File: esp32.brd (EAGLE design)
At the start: 123.5 x 80.4 mm, 12 parts, among them IC1 LM1117IMPX-3.3, U1 ESP32MOD

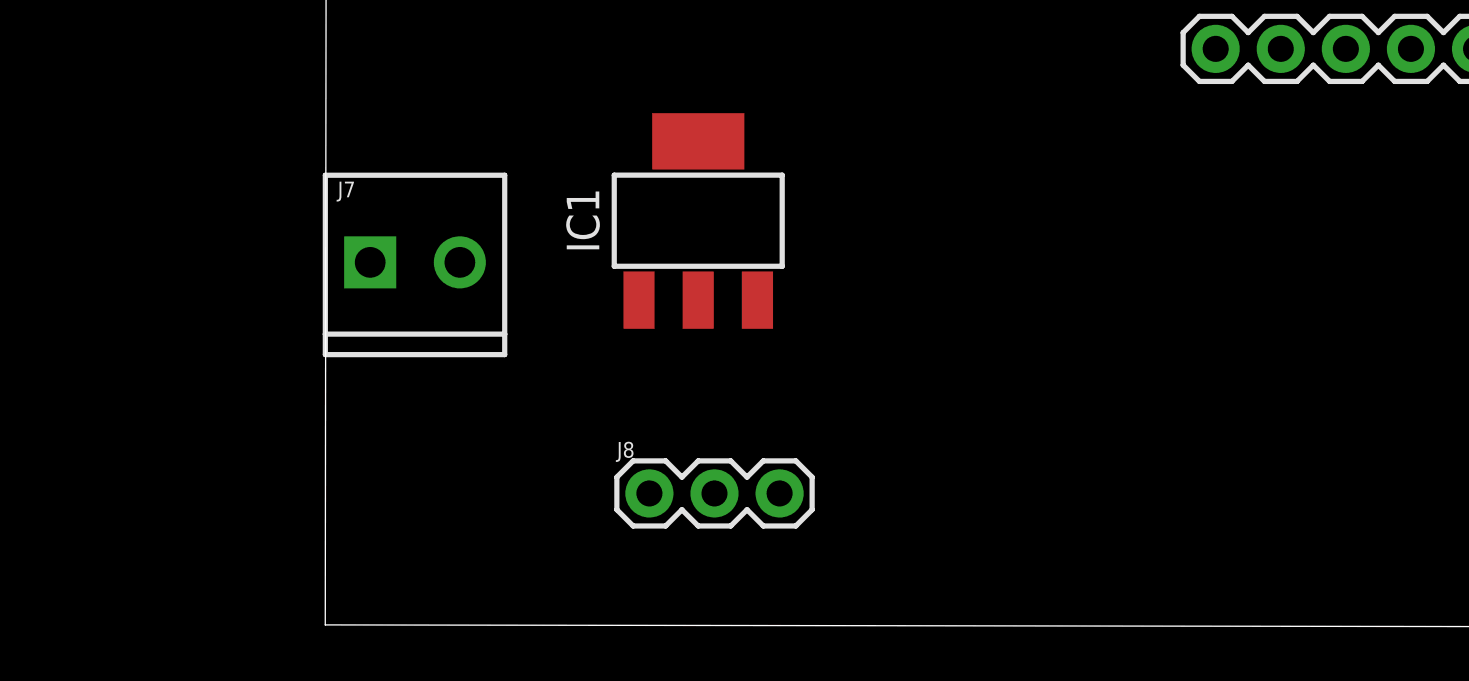
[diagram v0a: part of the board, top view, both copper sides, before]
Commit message: Added the reset circuitry
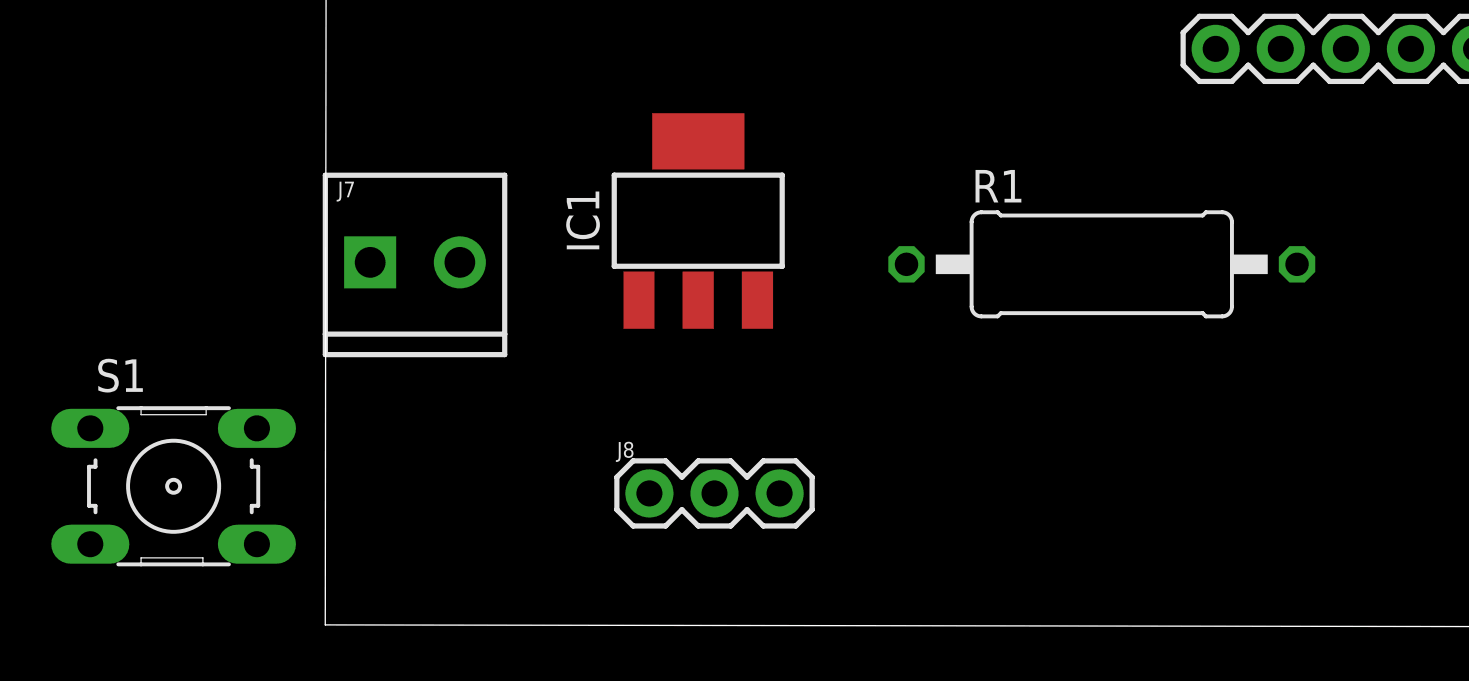
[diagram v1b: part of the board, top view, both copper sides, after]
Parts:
- added R1: (no value), rcl:0411/15
- added S1: (no value), switch-omron:B3F-10XX
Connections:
- removed net N$4: J1.13, J4.13, U1.2
- removed net N$5: J1.12, J4.12, U1.3
- new net RST: J1.12, J4.12, R1.2, S1.1, S1.2, U1.3
- net 3.3V: now also J1.13, J4.13, R1.1, U1.2
- net GND: now also S1.3, S1.4
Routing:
- net N$4: track 9.35 -> 0.00 mm
- net 3.3V: track 0.00 -> 9.35 mm
- net RST: track 0.00 -> 8.82 mm
- net N$5: track 8.82 -> 0.00 mm
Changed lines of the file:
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@@
 </element>
 <element name="J8" library="SparkFun-Connectors" package="1X03" value="" x="11.1252" y="16.891"/>
+<element name="R1" library="rcl" package="0411/15" value="" x="28.7782" y="25.8318"/>
+<element name="S1" library="switch-omron" package="B3F-10XX" value="" x="-7.4422" y="17.1704">
+<attribute name="OC_FARNELL" value="176432" x="-7.4422" y="17.1704" size="1.778" layer="27" display="off"/>
+<attribute name="MPN" value="B3F-1000" x="-7.4422" y="17.1704" size="1.778" layer="27" display="off"/>
+<attribute name="OC_NEWARK" value="36M3542" x="-7.4422" y="17.1704" size="1.778" layer="27" display="off"/>
+<attribute name="MF" value="" x="-7.4422" y="17.1704" size="1.778" layer="27" display="off"/>
+</element>
 </elements>
 <signals>
@@
 <contactref element="C1" pad="1"/>
 <contactref element="J8" pad="1"/>
+<contactref element="S1" pad="3"/>
+<contactref element="S1" pad="4"/>
 <wire x1="60.96" y1="77.216" x2="72.898" y2="77.2922" width="0" layer="19" extent="1-1"/>
 <wire x1="44.444" y1="64.116" x2="53.924" y2="71.806" width="0" layer="19" extent="1-1"/>
@@
 <wire x1="14.097" y1="77.4954" x2="27.686" y2="77.47" width="0" layer="19" extent="1-1"/>
 <wire x1="10.7192" y1="24.4346" x2="33.2232" y2="34.2392" width="0" layer="19" extent="1-1"/>
+<wire x1="11.1252" y1="16.891" x2="10.7192" y2="24.4346" width="0" layer="19" extent="1-1"/>
 <wire x1="0.2286" y1="25.908" x2="10.7192" y2="24.4346" width="0" layer="19" extent="1-1"/>
+<wire x1="-4.191" y1="14.9098" x2="0.2286" y2="25.908" width="0" layer="19" extent="1-1"/>
+<wire x1="-10.6934" y1="14.9098" x2="-4.191" y2="14.9098" width="0" layer="19" extent="1-1"/>
 <wire x1="6.9342" y1="39.6494" x2="0.2286" y2="25.908" width="0" layer="19" extent="1-1"/>
 <wire x1="7.7724" y1="47.9806" x2="6.9342" y2="39.6494" width="0" layer="19" extent="1-1"/>
-<wire x1="11.1252" y1="16.891" x2="0.2286" y2="25.908" width="0" layer="19" extent="1-1"/>
-</signal>
-<signal name="N$4">
-<contactref element="J1" pad="13"/>
-<contactref element="U1" pad="2"/>
-<wire x1="32.22625" y1="70.64375" x2="35.08375" y2="70.64375" width="0.5842" layer="1"/>
-<wire x1="27.94" y1="74.93" x2="32.22625" y2="70.64375" width="0.5842" layer="1"/>
-<wire x1="27.686" y1="74.93" x2="27.94" y2="74.93" width="0.5842" layer="1"/>
-<wire x1="35.08375" y1="70.64375" x2="35.224" y2="70.536" width="0.5842" layer="1"/>
-<contactref element="J4" pad="13"/>
-<wire x1="14.097" y1="74.9554" x2="27.686" y2="74.93" width="0" layer="19" extent="1-1"/>
-</signal>
-<signal name="N$5">
+</signal>
+<signal name="RST">
 <contactref element="J1" pad="12"/>
 <contactref element="U1" pad="3"/>
@@
 <wire x1="35.08375" y1="69.37375" x2="35.224" y2="69.266" width="0.5842" layer="1"/>
 <contactref element="J4" pad="12"/>
+<contactref element="R1" pad="2"/>
+<contactref element="S1" pad="1"/>
+<contactref element="S1" pad="2"/>
 <wire x1="14.097" y1="72.4154" x2="27.686" y2="72.39" width="0" layer="19" extent="1-1"/>
+<wire x1="36.3982" y1="25.8318" x2="35.224" y2="69.266" width="0" layer="19" extent="1-1"/>
+<wire x1="-4.191" y1="19.431" x2="36.3982" y2="25.8318" width="0" layer="19" extent="1-1"/>
+<wire x1="-10.6934" y1="19.431" x2="-4.191" y2="19.431" width="0" layer="19" extent="1-1"/>
 </signal>
 <signal name="N$2">
@@
 <contactref element="C2" pad="2"/>
 <contactref element="J8" pad="2"/>
+<contactref element="R1" pad="1"/>
+<contactref element="J1" pad="13"/>
+<contactref element="U1" pad="2"/>
+<wire x1="32.22625" y1="70.64375" x2="35.08375" y2="70.64375" width="0.5842" layer="1"/>
+<wire x1="27.94" y1="74.93" x2="32.22625" y2="70.64375" width="0.5842" layer="1"/>
+<wire x1="27.686" y1="74.93" x2="27.94" y2="74.93" width="0.5842" layer="1"/>
+<wire x1="35.08375" y1="70.64375" x2="35.224" y2="70.536" width="0.5842" layer="1"/>
+<contactref element="J4" pad="13"/>
+<wire x1="14.097" y1="74.9554" x2="27.686" y2="74.93" width="0" layer="19" extent="1-1"/>
+<wire x1="9.7282" y1="39.6494" x2="14.097" y2="74.9554" width="0" layer="19" extent="1-1"/>
 <wire x1="13.0302" y1="30.6326" x2="9.7282" y2="39.6494" width="0" layer="19" extent="1-1"/>
 <wire x1="13.0302" y1="24.4346" x2="13.0302" y2="30.6326" width="0" layer="19" extent="1-1"/>
 <wire x1="13.6652" y1="16.891" x2="13.0302" y2="24.4346" width="0" layer="19" extent="1-1"/>
+<wire x1="21.1582" y1="25.8318" x2="13.0302" y2="24.4346" width="0" layer="19" extent="1-1"/>
 </signal>
 </signals>

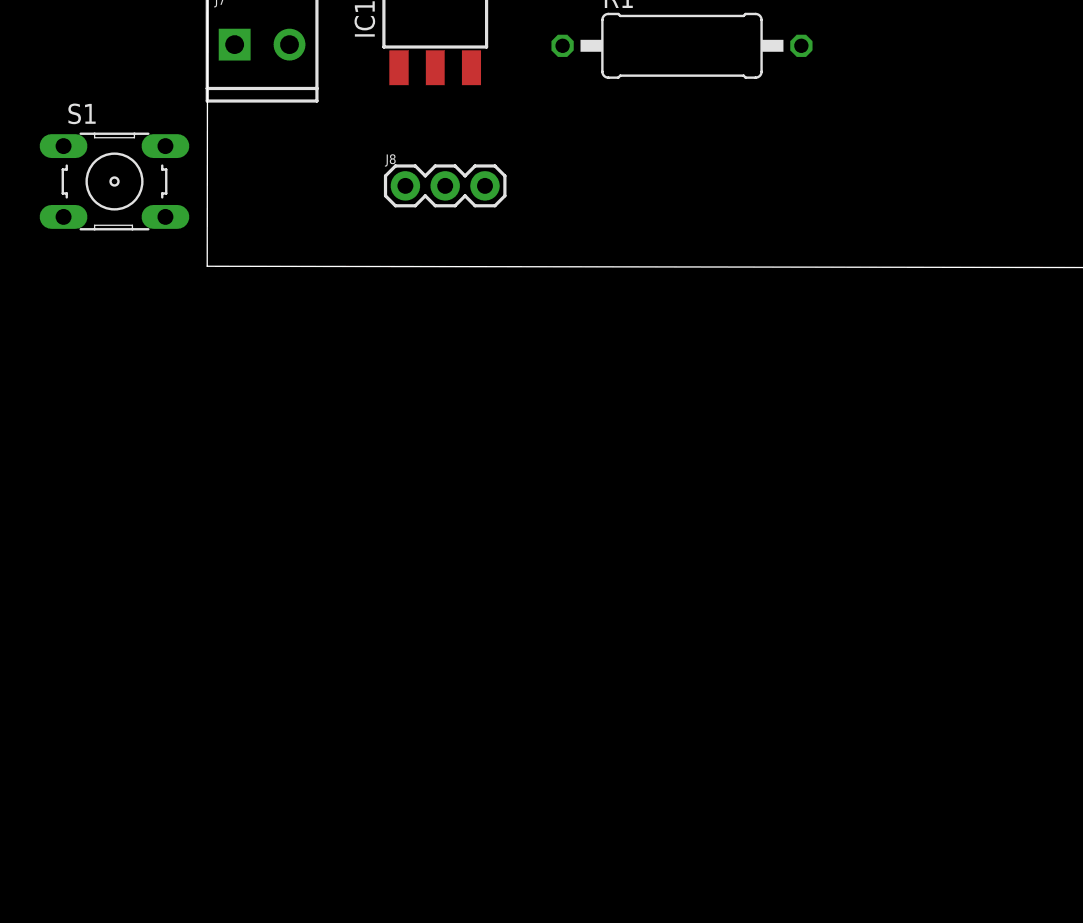
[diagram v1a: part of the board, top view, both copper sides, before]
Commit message: Added all the GPIO strapping bias resistors
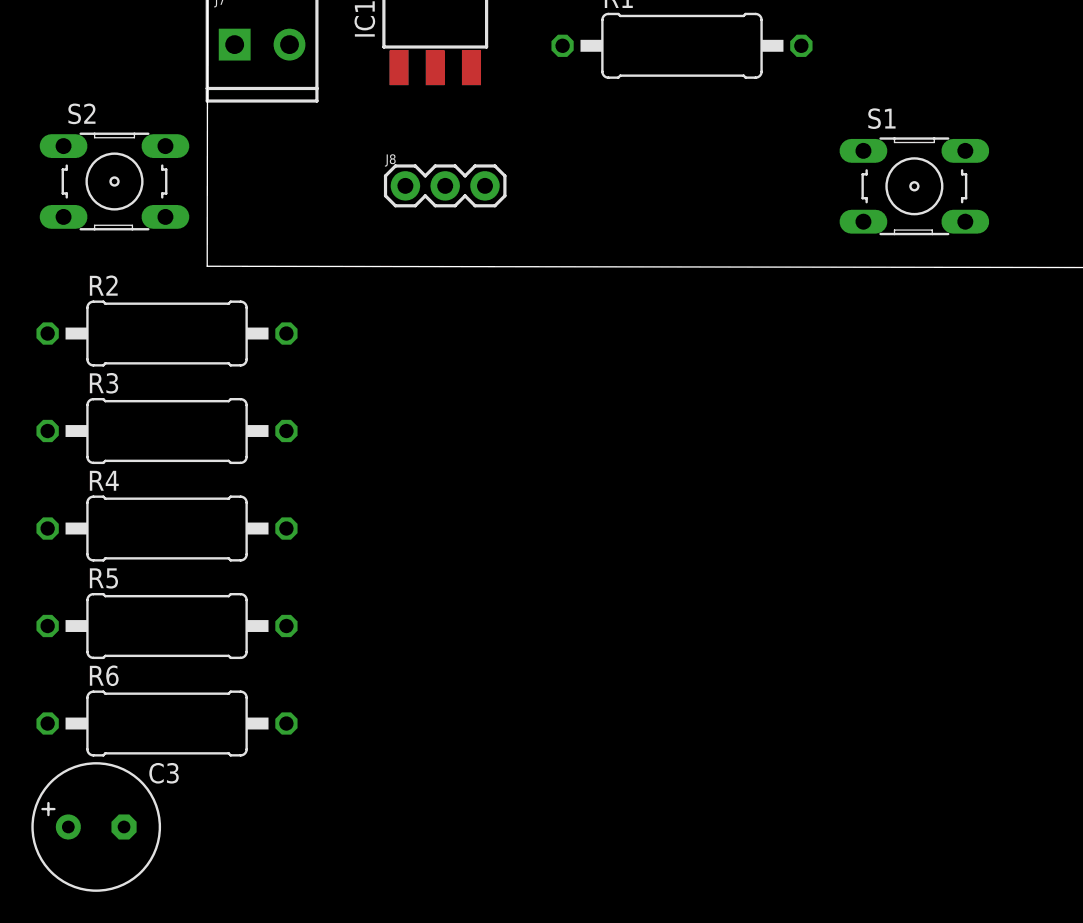
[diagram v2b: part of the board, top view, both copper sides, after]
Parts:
- added C3: (no value), rcl:E3,5-8
- added R2, R3, R4, R5, R6: 4.7k, rcl:0411/15
- added S2: (no value), switch-omron:B3F-10XX
- R1: value (none) -> 4.7k
- moved S1 51.1 mm to (43.6, 16.9)
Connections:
- net 3.3V: now also C3.+, R2.2, R5.1, R6.2
- net GND: now also C3.-, R3.2, R4.1, S2.3, S2.4
- net N$14: now also R4.2
- net N$19: now also R6.1
- net N$28: now also R2.1, S2.1, S2.2
- net N$37: now also R5.2
- net N$38: now also R3.1
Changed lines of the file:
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@@
 </element>
 <element name="J8" library="SparkFun-Connectors" package="1X03" value="" x="11.1252" y="16.891"/>
-<element name="R1" library="rcl" package="0411/15" value="" x="28.7782" y="25.8318"/>
-<element name="S1" library="switch-omron" package="B3F-10XX" value="" x="-7.4422" y="17.1704">
+<element name="R1" library="rcl" package="0411/15" value="4.7k" x="28.7782" y="25.8318"/>
+<element name="S1" library="switch-omron" package="B3F-10XX" value="" x="43.6118" y="16.8656">
+<attribute name="OC_FARNELL" value="176432" x="43.6118" y="16.8656" size="1.778" layer="27" display="off"/>
+<attribute name="MPN" value="B3F-1000" x="43.6118" y="16.8656" size="1.778" layer="27" display="off"/>
+<attribute name="OC_NEWARK" value="36M3542" x="43.6118" y="16.8656" size="1.778" layer="27" display="off"/>
+<attribute name="MF" value="" x="43.6118" y="16.8656" size="1.778" layer="27" display="off"/>
+</element>
+<element name="S2" library="switch-omron" package="B3F-10XX" value="" x="-7.4422" y="17.1704">
 <attribute name="OC_FARNELL" value="176432" x="-7.4422" y="17.1704" size="1.778" layer="27" display="off"/>
 <attribute name="MPN" value="B3F-1000" x="-7.4422" y="17.1704" size="1.778" layer="27" display="off"/>
@@
 <attribute name="MF" value="" x="-7.4422" y="17.1704" size="1.778" layer="27" display="off"/>
 </element>
+<element name="R2" library="rcl" package="0411/15" value="4.7k" x="-4.0894" y="7.4676"/>
+<element name="R3" library="rcl" package="0411/15" value="4.7k" x="-4.0894" y="1.2446"/>
+<element name="R4" library="rcl" package="0411/15" value="4.7k" x="-4.0894" y="-4.9784"/>
+<element name="R5" library="rcl" package="0411/15" value="4.7k" x="-4.0894" y="-11.2014"/>
+<element name="R6" library="rcl" package="0411/15" value="4.7k" x="-4.0894" y="-17.4244"/>
+<element name="C3" library="rcl" package="E3,5-8" value="" x="-8.6106" y="-24.0284"/>
 </elements>
 <signals>
@@
 <contactref element="S1" pad="3"/>
 <contactref element="S1" pad="4"/>
+<contactref element="S2" pad="4"/>
+<contactref element="S2" pad="3"/>
+<contactref element="R3" pad="2"/>
+<contactref element="R4" pad="1"/>
+<contactref element="C3" pad="-"/>
 <wire x1="60.96" y1="77.216" x2="72.898" y2="77.2922" width="0" layer="19" extent="1-1"/>
 <wire x1="44.444" y1="64.116" x2="53.924" y2="71.806" width="0" layer="19" extent="1-1"/>
@@
 <wire x1="33.2232" y1="34.2392" x2="33.274" y2="43.434" width="0" layer="19" extent="1-1"/>
 <wire x1="14.097" y1="77.4954" x2="27.686" y2="77.47" width="0" layer="19" extent="1-1"/>
+<wire x1="40.3606" y1="14.605" x2="33.2232" y2="34.2392" width="0" layer="19" extent="1-1"/>
+<wire x1="46.863" y1="14.605" x2="40.3606" y2="14.605" width="0" layer="19" extent="1-1"/>
 <wire x1="10.7192" y1="24.4346" x2="33.2232" y2="34.2392" width="0" layer="19" extent="1-1"/>
 <wire x1="11.1252" y1="16.891" x2="10.7192" y2="24.4346" width="0" layer="19" extent="1-1"/>
@@
 <wire x1="6.9342" y1="39.6494" x2="0.2286" y2="25.908" width="0" layer="19" extent="1-1"/>
 <wire x1="7.7724" y1="47.9806" x2="6.9342" y2="39.6494" width="0" layer="19" extent="1-1"/>
+<wire x1="3.5306" y1="1.2446" x2="-4.191" y2="14.9098" width="0" layer="19" extent="1-1"/>
+<wire x1="-11.7094" y1="-4.9784" x2="3.5306" y2="1.2446" width="0" layer="19" extent="1-1"/>
+<wire x1="-6.8326" y1="-24.0284" x2="-11.7094" y2="-4.9784" width="0" layer="19" extent="1-1"/>
 </signal>
 <signal name="RST">
@@
 <wire x1="14.097" y1="72.4154" x2="27.686" y2="72.39" width="0" layer="19" extent="1-1"/>
 <wire x1="36.3982" y1="25.8318" x2="35.224" y2="69.266" width="0" layer="19" extent="1-1"/>
-<wire x1="-4.191" y1="19.431" x2="36.3982" y2="25.8318" width="0" layer="19" extent="1-1"/>
-<wire x1="-10.6934" y1="19.431" x2="-4.191" y2="19.431" width="0" layer="19" extent="1-1"/>
+<wire x1="46.863" y1="19.1262" x2="36.3982" y2="25.8318" width="0" layer="19" extent="1-1"/>
+<wire x1="40.3606" y1="19.1262" x2="46.863" y2="19.1262" width="0" layer="19" extent="1-1"/>
 </signal>
 <signal name="N$2">
@@
 <wire x1="35.08375" y1="55.245" x2="35.224" y2="55.296" width="0.5842" layer="1"/>
 <contactref element="J4" pad="1"/>
+<contactref element="R4" pad="2"/>
 <wire x1="14.097" y1="44.4754" x2="27.686" y2="44.45" width="0" layer="19" extent="1-1"/>
+<wire x1="3.5306" y1="-4.9784" x2="14.097" y2="44.4754" width="0" layer="19" extent="1-1"/>
 </signal>
 <signal name="N$22">
@@
 <wire x1="60.96" y1="54.45125" x2="60.96" y2="54.356" width="0.5842" layer="1"/>
 <contactref element="J5" pad="10"/>
+<contactref element="R6" pad="1"/>
 <wire x1="60.96" y1="54.356" x2="72.898" y2="54.4322" width="0" layer="19" extent="1-1"/>
+<wire x1="-11.7094" y1="-17.4244" x2="53.975" y2="60.325" width="0" layer="19" extent="1-1"/>
 </signal>
 <signal name="N$15">
@@
 <wire x1="60.96" y1="44.29125" x2="60.96" y2="44.196" width="0.5842" layer="1"/>
 <contactref element="J5" pad="14"/>
+<contactref element="R2" pad="1"/>
+<contactref element="S2" pad="1"/>
+<contactref element="S2" pad="2"/>
 <wire x1="60.96" y1="44.196" x2="72.898" y2="44.2722" width="0" layer="19" extent="1-1"/>
+<wire x1="-4.191" y1="19.431" x2="53.975" y2="50.95875" width="0" layer="19" extent="1-1"/>
+<wire x1="-10.6934" y1="19.431" x2="-4.191" y2="19.431" width="0" layer="19" extent="1-1"/>
+<wire x1="-11.7094" y1="7.4676" x2="-10.6934" y2="19.431" width="0" layer="19" extent="1-1"/>
 </signal>
 <signal name="N$30">
@@
 <wire x1="53.49875" y1="43.4975" x2="53.594" y2="43.434" width="0.5842" layer="1"/>
 <contactref element="J6" pad="2"/>
+<contactref element="R5" pad="2"/>
 <wire x1="53.5432" y1="34.2392" x2="53.594" y2="43.434" width="0" layer="19" extent="1-1"/>
+<wire x1="3.5306" y1="-11.2014" x2="53.5432" y2="34.2392" width="0" layer="19" extent="1-1"/>
 </signal>
 <signal name="N$38">
@@
 <wire x1="56.03875" y1="43.4975" x2="56.134" y2="43.434" width="0.5842" layer="1"/>
 <contactref element="J6" pad="1"/>
+<contactref element="R3" pad="1"/>
 <wire x1="56.0832" y1="34.2392" x2="56.134" y2="43.434" width="0" layer="19" extent="1-1"/>
+<wire x1="-11.7094" y1="1.2446" x2="56.0832" y2="34.2392" width="0" layer="19" extent="1-1"/>
 </signal>
 <signal name="N$1">
@@
 <wire x1="35.08375" y1="70.64375" x2="35.224" y2="70.536" width="0.5842" layer="1"/>
 <contactref element="J4" pad="13"/>
+<contactref element="R2" pad="2"/>
+<contactref element="R5" pad="1"/>
+<contactref element="R6" pad="2"/>
+<contactref element="C3" pad="+"/>
 <wire x1="14.097" y1="74.9554" x2="27.686" y2="74.93" width="0" layer="19" extent="1-1"/>
 <wire x1="9.7282" y1="39.6494" x2="14.097" y2="74.9554" width="0" layer="19" extent="1-1"/>
@@
 <wire x1="13.6652" y1="16.891" x2="13.0302" y2="24.4346" width="0" layer="19" extent="1-1"/>
 <wire x1="21.1582" y1="25.8318" x2="13.0302" y2="24.4346" width="0" layer="19" extent="1-1"/>
+<wire x1="3.5306" y1="7.4676" x2="13.6652" y2="16.891" width="0" layer="19" extent="1-1"/>
+<wire x1="-11.7094" y1="-11.2014" x2="3.5306" y2="7.4676" width="0" layer="19" extent="1-1"/>
+<wire x1="-10.3886" y1="-24.0284" x2="-11.7094" y2="-11.2014" width="0" layer="19" extent="1-1"/>
+<wire x1="3.5306" y1="-17.4244" x2="-10.3886" y2="-24.0284" width="0" layer="19" extent="1-1"/>
 </signal>
 </signals>
